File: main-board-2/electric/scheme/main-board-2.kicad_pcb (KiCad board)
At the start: 2 copper layers, 85 x 56 mm, 122 parts, among them K1 power-switch, K2 usb-power-switch, P1 batt, P10 rst, P11 screw-1, P13 screw-2, P14 gpio-big, P15 gpio-small, P16 moto-1, P17 moto-2, P3 trigger-btn, P4 CONN_3X2, P7 bootloader, P8 cross board conn, P9 rst, Q1 IRLML2244, Q10 IRLML2244, Q11 sot223, Q12 bc857, Q13 irlml2244, Q2 BC847, Q3 IRLML2244, Q4 IRLML2244, Q5 BC847, Q6 BC847, Q7 BC847, Q8 BC847, Q9 IRLML2244, U1 LM317AEMP, U2 LM317AT, U3 LM317AEMP, U4 LM317AT, U5 LM293, U6 L298, U7 MINI-USB-B, X1 8MHz

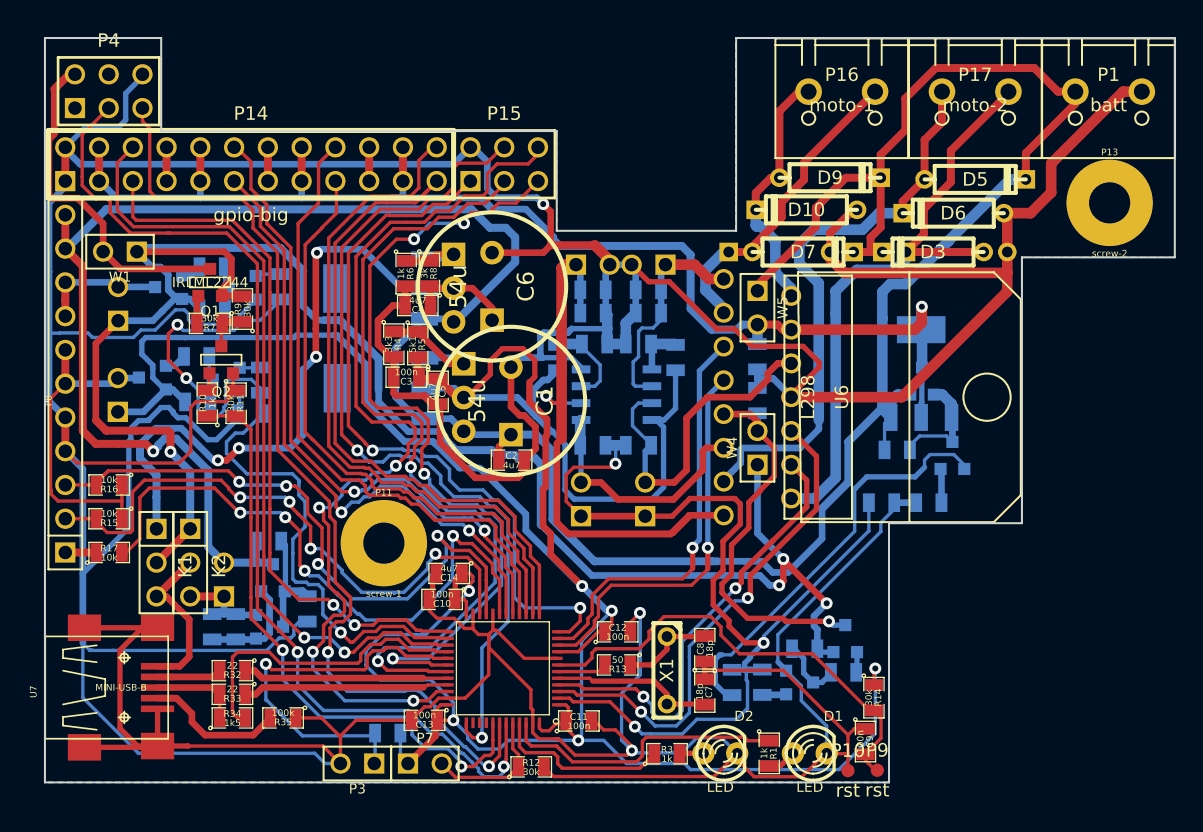
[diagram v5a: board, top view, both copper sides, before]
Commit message: Places zones and made thermal take zones under regulators.
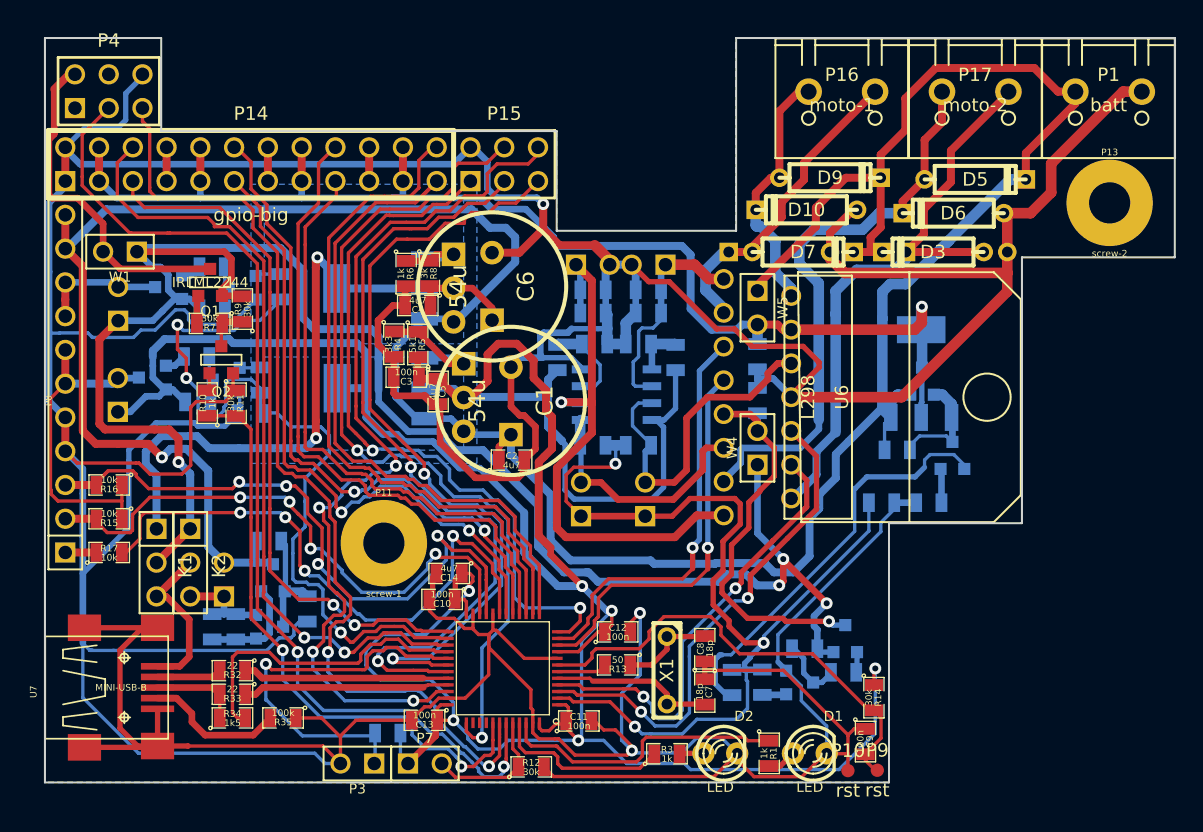
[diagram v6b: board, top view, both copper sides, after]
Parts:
- U1, U3: value LM317AEMP -> MY_LM317EMP
- U2, U4: value LM317AT -> MY_LM317T
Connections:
- C4 pad 1: N-0000085 (its old number) -> N-0000083
- C6 pad 1: N-0000085 (its old number) -> N-0000083
- K1 pad 1: N-0000085 (its old number) -> N-0000083
- R8 pad 2: N-0000085 (its old number) -> N-0000083
- U1 pad 4: (no net) -> VDD
- U3 pad 2: N-0000085 (its old number) -> N-0000083
- U3 pad 4: (no net) -> N-0000083
- U4 pad 2: N-0000085 (its old number) -> N-0000083
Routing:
- net N-0000085 (its old number): track 55.1 -> 0.00 mm, vias 4 -> 0
- net N-0000083: track 0.00 -> 53.3 mm, vias 0 -> 2
- net /cur-sense-2: track 55.4 -> 42.5 mm
- net VDD: track 229.5 -> 233.2 mm
- net /swd-io: track 71.1 -> 68.2 mm
- net /addon-trigger: track 46.7 -> 44.3 mm
- net /rx: track 62.7 -> 60.3 mm
- net /tx: track 62.0 -> 59.9 mm, vias 4 -> 2
- net /addon-pwr-en: track 60.6 -> 58.9 mm
- net GND: track 566.9 -> 565.6 mm
- net /+5V: track 142.0 -> 143.0 mm
- net /out4: track 45.9 -> 45.0 mm
- net /gpio-1: track 53.5 -> 52.5 mm
- net /gpio-2: track 47.5 -> 48.3 mm
- net /scl-rpi: track 72.8 -> 73.6 mm
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- added copper zone on B.Cu, net N-0000083
- added copper zone on B.Cu, net VDD

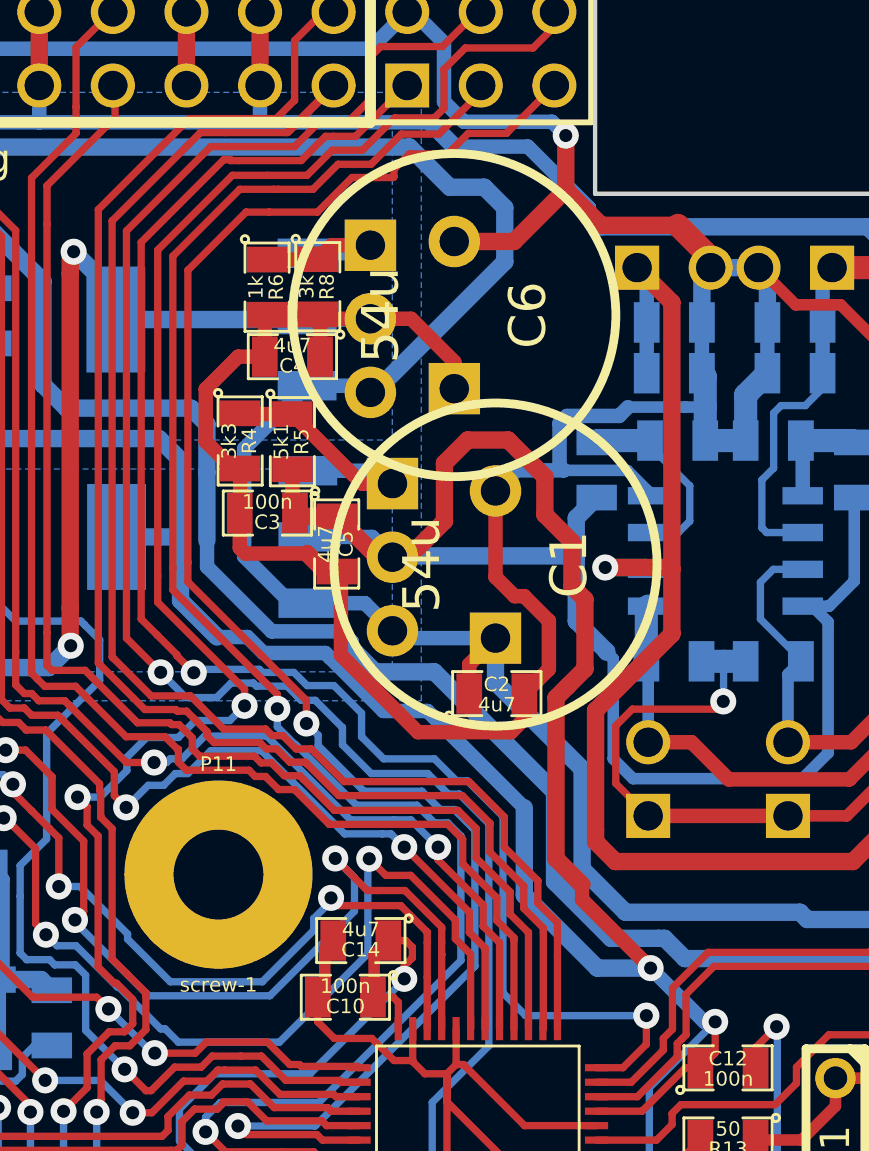
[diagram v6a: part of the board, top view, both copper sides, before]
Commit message: Displaced TO-220 regulators.
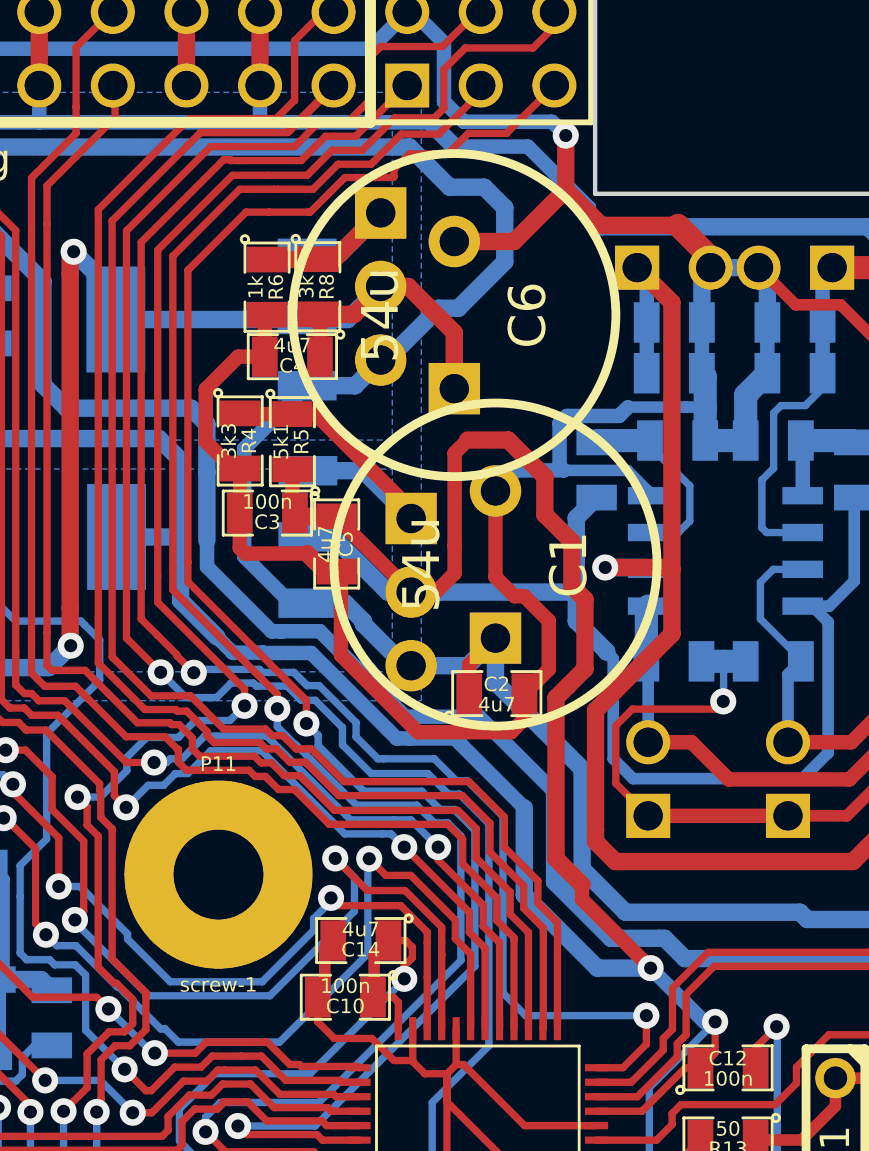
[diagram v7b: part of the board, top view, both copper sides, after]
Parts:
- moved U2 1.37 mm to (175.7, 153.2)
- moved U4 1.17 mm to (174.6, 142.7)
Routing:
- net VDD: track 233.2 -> 236.0 mm
- net N-0000085: track 9.37 -> 11.8 mm
- net N-0000083: track 53.3 -> 55.6 mm
- net /batt+: track 230.8 -> 232.7 mm
- net N-0000084: track 6.07 -> 7.71 mm

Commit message: Little improvements.
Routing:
- net /pwrVs: track 95.4 -> 104.3 mm
- net N-0000083: track 55.6 -> 61.2 mm
- net /+5V: track 142.9 -> 139.4 mm
- net /cur-sense-2: track 42.5 -> 40.0 mm
- net /batt+: track 232.7 -> 235.1 mm
- net GND: track 565.6 -> 566.7 mm
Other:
- board text added: "G"
- board text added: "http://grambo-pi.com"
